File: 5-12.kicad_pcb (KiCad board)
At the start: 2 copper layers, 266.7 x 95.2 mm, 136 parts, among them SW1 SW_Push, U1 ATmega32U4-AU, Y1 16MHz

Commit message: Routed left half of bottom row
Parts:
- moved D60 120.3 mm to (158.8, 137.8), turned to 270 degrees
- moved D5 105.1 mm to (132.2, 137.8), turned to 270 degrees
- moved D55 103.9 mm to (156.3, 137.8), turned to 270 degrees
- moved D10 88.9 mm to (134.6, 137.8), turned to 270 degrees
- moved D50 87.7 mm to (153.9, 137.8), turned to 270 degrees
- moved D15 72.9 mm to (137.0, 137.8), turned to 270 degrees
- moved D45 71.8 mm to (151.5, 137.8), turned to 270 degrees
- moved D20 57.2 mm to (139.4, 137.8), turned to 270 degrees
- moved D40 56.1 mm to (149.1, 137.8), turned to 270 degrees
- moved D25 42.3 mm to (141.9, 137.8), turned to 270 degrees
- moved D35 31.4 mm to (146.7, 137.8), turned to 270 degrees
- moved D30 20.1 mm to (144.3, 137.8), turned to 270 degrees
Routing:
- net Net-(D5-Pad2): track 0.00 -> 115.4 mm
- net Net-(D10-Pad2): track 0.00 -> 100.2 mm
- net Net-(D15-Pad2): track 0.00 -> 84.0 mm
- net Net-(D20-Pad2): track 0.00 -> 75.6 mm
- net Net-(D25-Pad2): track 0.00 -> 56.3 mm
- net Net-(D35-Pad2): track 0.00 -> 33.0 mm
- net Net-(D30-Pad2): track 0.00 -> 28.4 mm
- net Row5: track 0.00 -> 26.5 mm
- net (no net): vias 0 -> 1

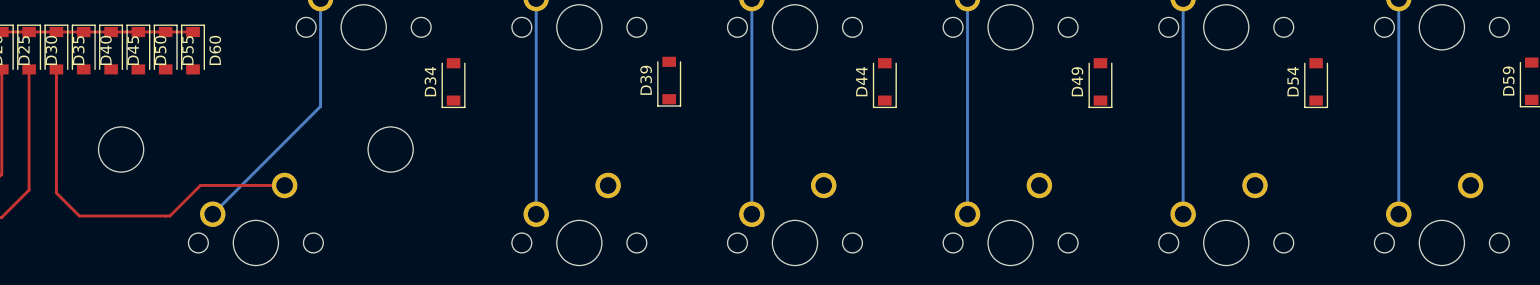
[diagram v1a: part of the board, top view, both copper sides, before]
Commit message: Finished routing bottom row to diode bank
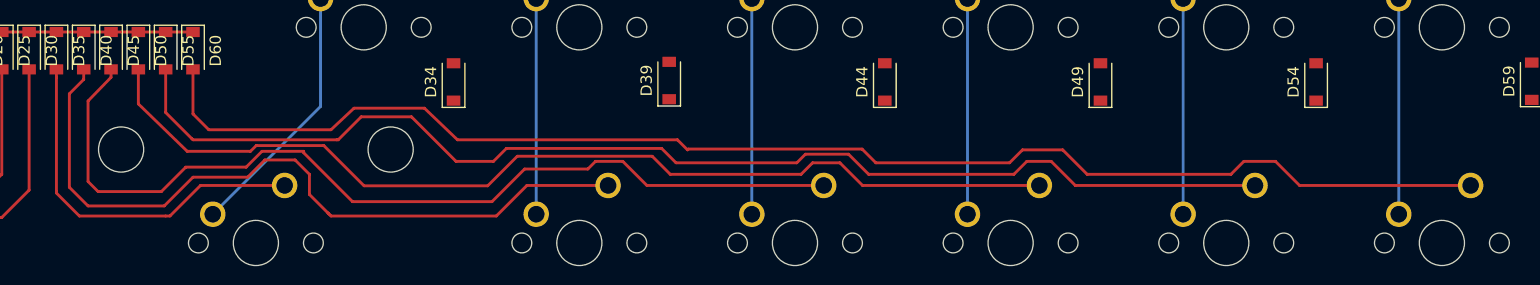
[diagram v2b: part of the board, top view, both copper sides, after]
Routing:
- net Net-(D60-Pad2): track 0.00 -> 122.9 mm
- net Net-(D55-Pad2): track 0.00 -> 106.9 mm
- net Net-(D50-Pad2): track 0.00 -> 89.0 mm
- net Net-(D45-Pad2): track 0.00 -> 81.8 mm
- net Net-(D40-Pad2): track 0.00 -> 65.2 mm
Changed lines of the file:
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@@
     (thickness 1.6)
     (drawings 8)
-    (tracks 275)
+    (tracks 366)
     (zones 0)
     (modules 136)
@@
   (segment (start 156.337 152.4) (end 156.718 152.4) (width 0.254) (layer F.Cu) (net 45))
   (segment (start 156.718 152.4) (end 159.41675 149.70125) (width 0.254) (layer F.Cu) (net 45))
+  (segment (start 195.42125 149.70125) (end 188.24575 149.70125) (width 0.254) (layer F.Cu) (net 50))
+  (segment (start 188.24575 149.70125) (end 185.547 152.4) (width 0.254) (layer F.Cu) (net 50))
+  (segment (start 170.942 152.4) (end 170.688 152.146) (width 0.254) (layer F.Cu) (net 50))
+  (segment (start 185.547 152.4) (end 170.942 152.4) (width 0.254) (layer F.Cu) (net 50))
+  (segment (start 170.78325 152.24125) (end 170.688 152.146) (width 0.254) (layer F.Cu) (net 50))
+  (segment (start 147.828 141.605) (end 147.828 149.86) (width 0.254) (layer F.Cu) (net 50))
+  (segment (start 149.479 151.511) (end 156.21 151.511) (width 0.254) (layer F.Cu) (net 50))
+  (segment (start 169.037 150.495) (end 170.688 152.146) (width 0.254) (layer F.Cu) (net 50))
+  (segment (start 149.098 140.335) (end 147.828 141.605) (width 0.254) (layer F.Cu) (net 50))
+  (segment (start 163.576 148.971) (end 165.1 147.447) (width 0.254) (layer F.Cu) (net 50))
+  (segment (start 147.828 149.86) (end 149.479 151.511) (width 0.254) (layer F.Cu) (net 50))
+  (segment (start 156.21 151.511) (end 158.75 148.971) (width 0.254) (layer F.Cu) (net 50))
+  (segment (start 149.098 139.444) (end 149.098 140.335) (width 0.254) (layer F.Cu) (net 50))
+  (segment (start 158.75 148.971) (end 163.576 148.971) (width 0.254) (layer F.Cu) (net 50))
+  (segment (start 165.1 147.447) (end 167.767 147.447) (width 0.254) (layer F.Cu) (net 50))
+  (segment (start 167.767 147.447) (end 169.037 148.717) (width 0.254) (layer F.Cu) (net 50))
+  (segment (start 169.037 148.717) (end 169.037 150.495) (width 0.254) (layer F.Cu) (net 50))
+  (segment (start 196.723 147.574) (end 198.85025 149.70125) (width 0.254) (layer F.Cu) (net 55))
+  (segment (start 194.31 147.574) (end 196.723 147.574) (width 0.254) (layer F.Cu) (net 55))
+  (segment (start 188.046751 148.249249) (end 193.634751 148.249249) (width 0.254) (layer F.Cu) (net 55))
+  (segment (start 172.847 151.13) (end 185.166 151.13) (width 0.254) (layer F.Cu) (net 55))
+  (segment (start 151.511 139.444) (end 151.511 140.148) (width 0.254) (layer F.Cu) (net 55))
+  (segment (start 198.85025 149.70125) (end 214.47125 149.70125) (width 0.254) (layer F.Cu) (net 55))
+  (segment (start 185.166 151.13) (end 188.046751 148.249249) (width 0.254) (layer F.Cu) (net 55))
+  (segment (start 151.511 140.148) (end 149.479 142.24) (width 0.254) (layer F.Cu) (net 55))
+  (segment (start 193.634751 148.249249) (end 194.31 147.574) (width 0.254) (layer F.Cu) (net 55))
+  (segment (start 149.479 142.24) (end 149.479 149.352) (width 0.254) (layer F.Cu) (net 55))
+  (segment (start 149.479 149.352) (end 150.368 150.241) (width 0.254) (layer F.Cu) (net 55))
+  (segment (start 158.115 148.082) (end 163.449 148.082) (width 0.254) (layer F.Cu) (net 55))
+  (segment (start 150.368 150.241) (end 155.956 150.241) (width 0.254) (layer F.Cu) (net 55))
+  (segment (start 164.846 146.685) (end 168.529 146.685) (width 0.254) (layer F.Cu) (net 55))
+  (segment (start 163.449 148.082) (end 164.846 146.685) (width 0.254) (layer F.Cu) (net 55))
+  (segment (start 155.956 150.241) (end 158.115 148.082) (width 0.254) (layer F.Cu) (net 55))
+  (segment (start 168.529 146.685) (end 168.529 146.812) (width 0.254) (layer F.Cu) (net 55))
+  (segment (start 168.529 146.812) (end 172.847 151.13) (width 0.254) (layer F.Cu) (net 55))
+  (segment (start 153.924 142.494) (end 153.924 139.446) (width 0.254) (layer F.Cu) (net 60))
+  (segment (start 158.242 146.685) (end 153.924 142.494) (width 0.254) (layer F.Cu) (net 60))
+  (segment (start 163.83 146.685) (end 158.242 146.685) (width 0.254) (layer F.Cu) (net 60))
+  (segment (start 164.338 146.177) (end 163.83 146.685) (width 0.254) (layer F.Cu) (net 60))
+  (segment (start 212.471 148.717) (end 200.914 148.717) (width 0.254) (layer F.Cu) (net 60))
+  (segment (start 170.307 146.177) (end 164.338 146.177) (width 0.254) (layer F.Cu) (net 60))
+  (segment (start 217.90025 149.70125) (end 215.9 147.701) (width 0.254) (layer F.Cu) (net 60))
+  (segment (start 215.9 147.701) (end 213.487 147.701) (width 0.254) (layer F.Cu) (net 60))
+  (segment (start 213.487 147.701) (end 212.471 148.717) (width 0.254) (layer F.Cu) (net 60))
+  (segment (start 200.914 148.717) (end 199.31699 147.11999) (width 0.254) (layer F.Cu) (net 60))
+  (segment (start 199.31699 147.11999) (end 187.39801 147.11999) (width 0.254) (layer F.Cu) (net 60))
+  (segment (start 233.52125 149.70125) (end 217.90025 149.70125) (width 0.254) (layer F.Cu) (net 60))
+  (segment (start 173.863 149.733) (end 170.307 146.177) (width 0.254) (layer F.Cu) (net 60))
+  (segment (start 187.39801 147.11999) (end 184.785 149.733) (width 0.254) (layer F.Cu) (net 60))
+  (segment (start 184.785 149.733) (end 173.863 149.733) (width 0.254) (layer F.Cu) (net 60))
+  (segment (start 156.337 139.446) (end 156.337 143.256) (width 0.254) (layer F.Cu) (net 65))
+  (segment (start 156.337 143.256) (end 158.623 145.542) (width 0.254) (layer F.Cu) (net 65))
+  (segment (start 158.623 145.542) (end 158.75 145.669) (width 0.254) (layer F.Cu) (net 65))
+  (segment (start 158.75 145.669) (end 171.45 145.669) (width 0.254) (layer F.Cu) (net 65))
+  (segment (start 171.577 145.669) (end 171.45 145.669) (width 0.254) (layer F.Cu) (net 65))
+  (segment (start 173.609 143.637) (end 171.577 145.669) (width 0.254) (layer F.Cu) (net 65))
+  (segment (start 178.054 143.637) (end 173.609 143.637) (width 0.254) (layer F.Cu) (net 65))
+  (segment (start 186.436 146.431) (end 185.293 147.574) (width 0.254) (layer F.Cu) (net 65))
+  (segment (start 232.41 147.574) (end 231.267 148.717) (width 0.254) (layer F.Cu) (net 65))
+  (segment (start 201.422 147.701) (end 200.152 146.431) (width 0.254) (layer F.Cu) (net 65))
+  (segment (start 181.991 147.574) (end 178.054 143.637) (width 0.254) (layer F.Cu) (net 65))
+  (segment (start 234.569 147.574) (end 232.41 147.574) (width 0.254) (layer F.Cu) (net 65))
+  (segment (start 236.69625 149.70125) (end 234.569 147.574) (width 0.254) (layer F.Cu) (net 65))
+  (segment (start 252.57125 149.70125) (end 236.69625 149.70125) (width 0.254) (layer F.Cu) (net 65))
+  (segment (start 218.44 148.717) (end 216.662 146.939) (width 0.254) (layer F.Cu) (net 65))
+  (segment (start 185.293 147.574) (end 181.991 147.574) (width 0.254) (layer F.Cu) (net 65))
+  (segment (start 216.662 146.939) (end 212.852 146.939) (width 0.254) (layer F.Cu) (net 65))
+  (segment (start 231.267 148.717) (end 218.44 148.717) (width 0.254) (layer F.Cu) (net 65))
+  (segment (start 200.152 146.431) (end 186.436 146.431) (width 0.254) (layer F.Cu) (net 65))
+  (segment (start 212.852 146.939) (end 212.09 147.701) (width 0.254) (layer F.Cu) (net 65))
+  (segment (start 212.09 147.701) (end 201.422 147.701) (width 0.254) (layer F.Cu) (net 65))
+  (segment (start 158.75 143.383) (end 158.75 139.446) (width 0.254) (layer F.Cu) (net 70))
+  (segment (start 172.974 142.875) (end 170.942 144.78) (width 0.254) (layer F.Cu) (net 70))
+  (segment (start 179.197 142.875) (end 172.974 142.875) (width 0.254) (layer F.Cu) (net 70))
+  (segment (start 182.118 145.669) (end 179.197 142.875) (width 0.254) (layer F.Cu) (net 70))
+  (segment (start 201.549 145.669) (end 182.118 145.669) (width 0.254) (layer F.Cu) (net 70))
+  (segment (start 202.438 146.558) (end 201.549 145.669) (width 0.254) (layer F.Cu) (net 70))
+  (segment (start 251.587 147.574) (end 250.444 148.717) (width 0.254) (layer F.Cu) (net 70))
+  (segment (start 202.51101 146.48499) (end 202.438 146.558) (width 0.254) (layer F.Cu) (net 70))
+  (segment (start 256.50825 149.70125) (end 254.381 147.574) (width 0.254) (layer F.Cu) (net 70))
+  (segment (start 170.942 144.78) (end 160.147 144.78) (width 0.254) (layer F.Cu) (net 70))
+  (segment (start 254.381 147.574) (end 251.587 147.574) (width 0.254) (layer F.Cu) (net 70))
+  (segment (start 250.444 148.717) (end 237.744 148.717) (width 0.254) (layer F.Cu) (net 70))
+  (segment (start 271.62125 149.70125) (end 256.50825 149.70125) (width 0.254) (layer F.Cu) (net 70))
+  (segment (start 235.585 146.558) (end 232.029 146.558) (width 0.254) (layer F.Cu) (net 70))
+  (segment (start 232.029 146.558) (end 230.886 147.701) (width 0.254) (layer F.Cu) (net 70))
+  (segment (start 160.147 144.78) (end 158.75 143.383) (width 0.254) (layer F.Cu) (net 70))
+  (segment (start 217.85899 146.48499) (end 202.51101 146.48499) (width 0.254) (layer F.Cu) (net 70))
+  (segment (start 230.886 147.701) (end 219.075 147.701) (width 0.254) (layer F.Cu) (net 70))
+  (segment (start 237.744 148.717) (end 235.585 146.558) (width 0.254) (layer F.Cu) (net 70))
+  (segment (start 219.075 147.701) (end 217.85899 146.48499) (width 0.254) (layer F.Cu) (net 70))
   (segment (start 152.53 78.246) (end 152.53 79.121) (width 0.381) (layer F.Cu) (net 71))
   (segment (start 147.30625 76.64975) (end 148.51199 77.85549) (width 0.381) (layer F.Cu) (net 71))

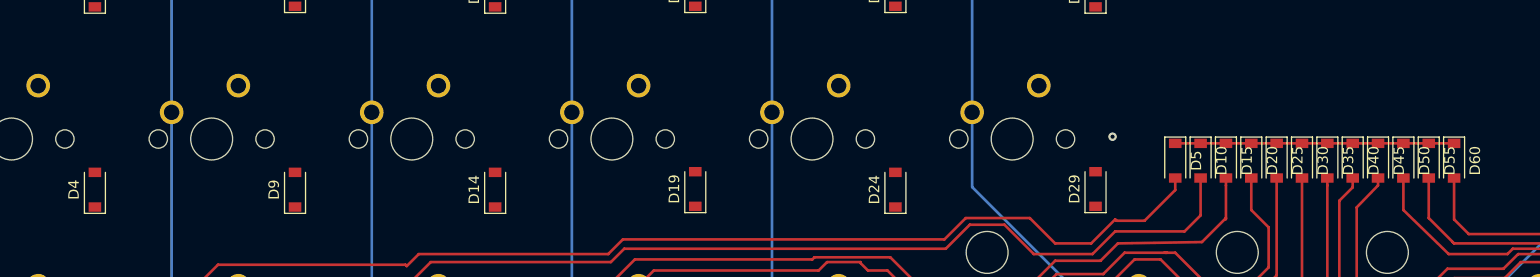
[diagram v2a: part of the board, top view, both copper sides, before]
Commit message: moved diodes of right side r4 into bank
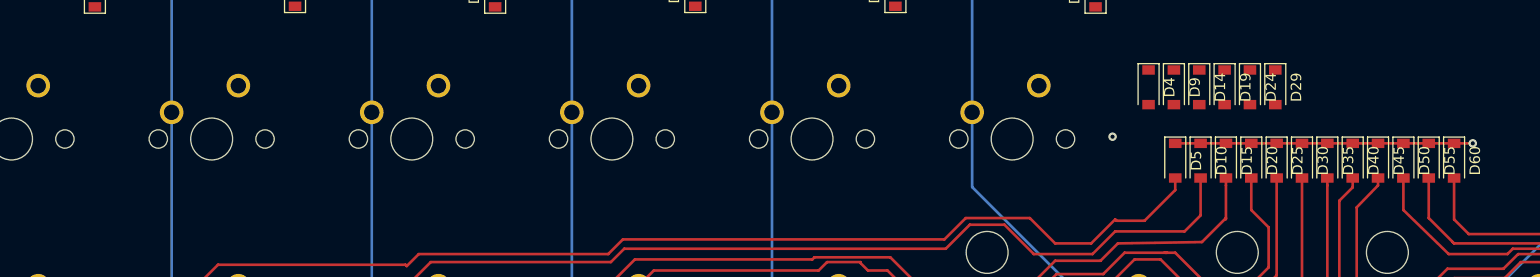
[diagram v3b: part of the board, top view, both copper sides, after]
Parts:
- moved D4 100.8 mm to (129.7, 130.8), turned to 270 degrees
- moved D9 84.2 mm to (132.1, 130.8), turned to 270 degrees
- moved D14 67.7 mm to (134.5, 130.8), turned to 270 degrees
- moved D19 51.3 mm to (136.9, 130.8), turned to 270 degrees
- moved D24 35.1 mm to (139.3, 130.8), turned to 270 degrees
- moved D29 19.7 mm to (141.7, 130.8), turned to 270 degrees
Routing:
- net Row5: track 26.5 -> 28.3 mm, vias 0 -> 1
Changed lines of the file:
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@@
     (thickness 1.6)
     (drawings 8)
-    (tracks 366)
+    (tracks 369)
     (zones 0)
     (modules 136)
@@
   )
   (module Diode_SMD:D_SOD-123 (layer F.Cu)
-    (at 124.61875 140.49375 90)
+    (at 141.732 130.809 270)
     (descr SOD-123)
     (tags SOD-123)
@@
       (effects (font (size 1 1) (thickness 0.15)))
     )
-    (pad 2 smd rect (at 1.65 0 90) (size 0.9 1.2) (layers F.Cu F.Paste F.Mask)
+    (pad 2 smd rect (at 1.65 0 270) (size 0.9 1.2) (layers F.Cu F.Paste F.Mask)
       (net 39 "Net-(D29-Pad2)"))
-    (pad 1 smd rect (at -1.65 0 90) (size 0.9 1.2) (layers F.Cu F.Paste F.Mask)
+    (pad 1 smd rect (at -1.65 0 270) (size 0.9 1.2) (layers F.Cu F.Paste F.Mask)
       (net 13 Row3))
     (model ${KISYS3DMOD}/Diode_SMD.3dshapes/D_SOD-123.wrl
@@
   )
   (module Diode_SMD:D_SOD-123 (layer F.Cu)
-    (at 105.56875 140.55625 90)
+    (at 139.319 130.81 270)
     (descr SOD-123)
     (tags SOD-123)
@@
       (effects (font (size 1 1) (thickness 0.15)))
     )
-    (pad 2 smd rect (at 1.65 0 90) (size 0.9 1.2) (layers F.Cu F.Paste F.Mask)
+    (pad 2 smd rect (at 1.65 0 270) (size 0.9 1.2) (layers F.Cu F.Paste F.Mask)
       (net 34 "Net-(D24-Pad2)"))
-    (pad 1 smd rect (at -1.65 0 90) (size 0.9 1.2) (layers F.Cu F.Paste F.Mask)
+    (pad 1 smd rect (at -1.65 0 270) (size 0.9 1.2) (layers F.Cu F.Paste F.Mask)
       (net 13 Row3))
     (model ${KISYS3DMOD}/Diode_SMD.3dshapes/D_SOD-123.wrl
@@
   )
   (module Diode_SMD:D_SOD-123 (layer F.Cu)
-    (at 86.51875 140.49375 90)
+    (at 136.906 130.811 270)
     (descr SOD-123)
     (tags SOD-123)
@@
       (effects (font (size 1 1) (thickness 0.15)))
     )
-    (pad 2 smd rect (at 1.65 0 90) (size 0.9 1.2) (layers F.Cu F.Paste F.Mask)
+    (pad 2 smd rect (at 1.65 0 270) (size 0.9 1.2) (layers F.Cu F.Paste F.Mask)
       (net 29 "Net-(D19-Pad2)"))
-    (pad 1 smd rect (at -1.65 0 90) (size 0.9 1.2) (layers F.Cu F.Paste F.Mask)
+    (pad 1 smd rect (at -1.65 0 270) (size 0.9 1.2) (layers F.Cu F.Paste F.Mask)
       (net 13 Row3))
     (model ${KISYS3DMOD}/Diode_SMD.3dshapes/D_SOD-123.wrl
@@
   )
   (module Diode_SMD:D_SOD-123 (layer F.Cu)
-    (at 67.46875 140.55625 90)
+    (at 134.493 130.811 270)
     (descr SOD-123)
     (tags SOD-123)
@@
       (effects (font (size 1 1) (thickness 0.15)))
     )
-    (pad 2 smd rect (at 1.65 0 90) (size 0.9 1.2) (layers F.Cu F.Paste F.Mask)
+    (pad 2 smd rect (at 1.65 0 270) (size 0.9 1.2) (layers F.Cu F.Paste F.Mask)
       (net 24 "Net-(D14-Pad2)"))
-    (pad 1 smd rect (at -1.65 0 90) (size 0.9 1.2) (layers F.Cu F.Paste F.Mask)
+    (pad 1 smd rect (at -1.65 0 270) (size 0.9 1.2) (layers F.Cu F.Paste F.Mask)
       (net 13 Row3))
     (model ${KISYS3DMOD}/Diode_SMD.3dshapes/D_SOD-123.wrl
@@
   )
   (module Diode_SMD:D_SOD-123 (layer F.Cu)
-    (at 48.41875 140.55625 90)
+    (at 132.08 130.811 270)
     (descr SOD-123)
     (tags SOD-123)
@@
       (effects (font (size 1 1) (thickness 0.15)))
     )
-    (pad 2 smd rect (at 1.65 0 90) (size 0.9 1.2) (layers F.Cu F.Paste F.Mask)
+    (pad 2 smd rect (at 1.65 0 270) (size 0.9 1.2) (layers F.Cu F.Paste F.Mask)
       (net 19 "Net-(D9-Pad2)"))
-    (pad 1 smd rect (at -1.65 0 90) (size 0.9 1.2) (layers F.Cu F.Paste F.Mask)
+    (pad 1 smd rect (at -1.65 0 270) (size 0.9 1.2) (layers F.Cu F.Paste F.Mask)
       (net 13 Row3))
     (model ${KISYS3DMOD}/Diode_SMD.3dshapes/D_SOD-123.wrl
@@
   )
   (module Diode_SMD:D_SOD-123 (layer F.Cu)
-    (at 29.36875 140.55625 90)
+    (at 129.667 130.81 270)
     (descr SOD-123)
     (tags SOD-123)
@@
       (effects (font (size 1 1) (thickness 0.15)))
     )
-    (pad 2 smd rect (at 1.65 0 90) (size 0.9 1.2) (layers F.Cu F.Paste F.Mask)
+    (pad 2 smd rect (at 1.65 0 270) (size 0.9 1.2) (layers F.Cu F.Paste F.Mask)
       (net 12 "Net-(D4-Pad2)"))
-    (pad 1 smd rect (at -1.65 0 90) (size 0.9 1.2) (layers F.Cu F.Paste F.Mask)
+    (pad 1 smd rect (at -1.65 0 270) (size 0.9 1.2) (layers F.Cu F.Paste F.Mask)
       (net 13 Row3))
     (model ${KISYS3DMOD}/Diode_SMD.3dshapes/D_SOD-123.wrl
@@
   (segment (start 158.748 136.144) (end 158.75 136.146) (width 0.254) (layer F.Cu) (net 15))
   (segment (start 132.207 136.144) (end 158.748 136.144) (width 0.254) (layer F.Cu) (net 15))
+  (via (at 160.528 136.144) (size 0.8) (drill 0.4) (layers F.Cu B.Cu) (net 15))
+  (segment (start 158.75 136.146) (end 160.526 136.146) (width 0.254) (layer F.Cu) (net 15))
+  (segment (start 160.526 136.146) (end 160.528 136.144) (width 0.254) (layer F.Cu) (net 15))
   (segment (start 134.62 143.002) (end 134.62 139.444) (width 0.254) (layer F.Cu) (net 20))
   (segment (start 79.756 146.177) (end 110.363 146.177) (width 0.254) (layer F.Cu) (net 20))
